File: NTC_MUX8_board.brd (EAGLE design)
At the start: 76.2 x 63.5 mm, 67 parts, among them IC1 NINA-B306-00B-00, IC2 INA126E, IC3 MCP6001T_SOT23, IC4 MAX8559ETAAA+T, J1 USB4105-GF-A, J2 1761681-7, J3 DM3CS-SF-PEJMS, J4 DNP, J7 52808-2071, U1 TMUX1208PWR, U2 TMUX1208PWR, U3 TMUX1208PWR, U4 TMUX1208PWR, X1 22-23-2021

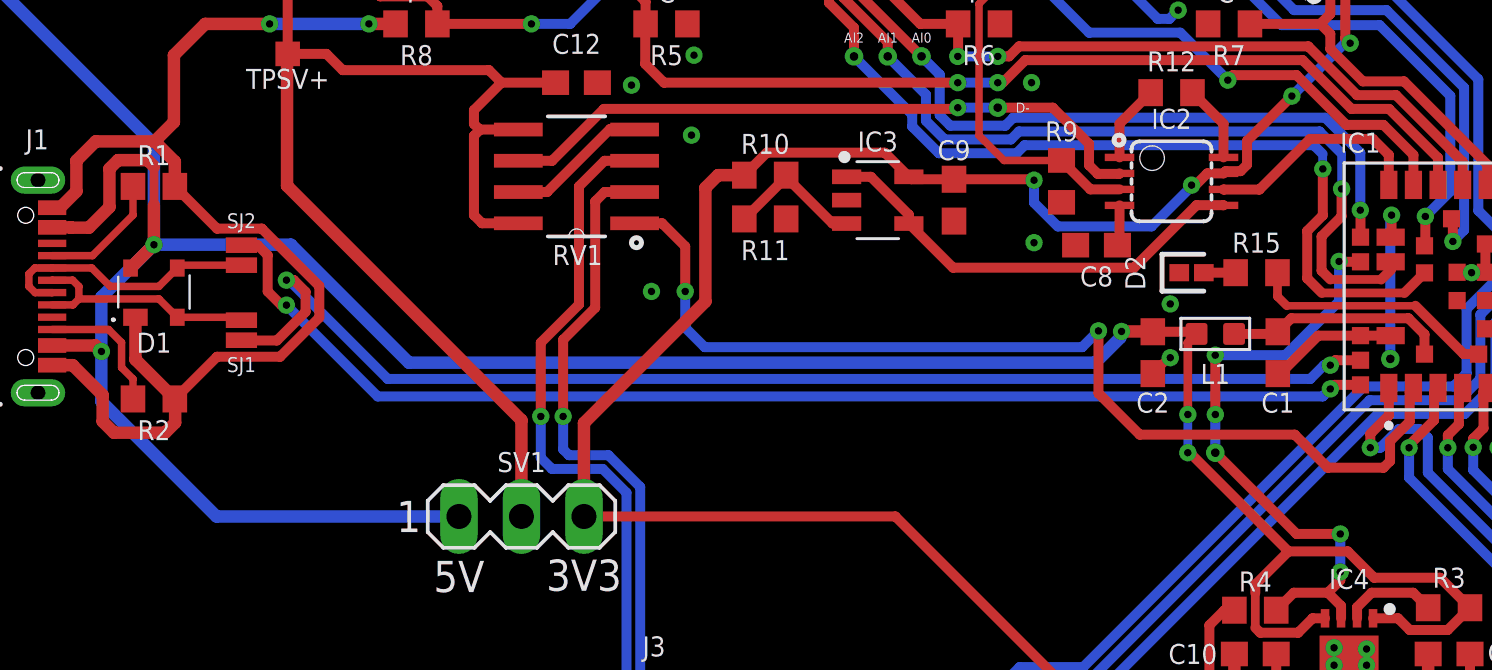
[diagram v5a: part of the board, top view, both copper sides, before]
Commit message: minor corrections
corrección v en seguidor
y pistas
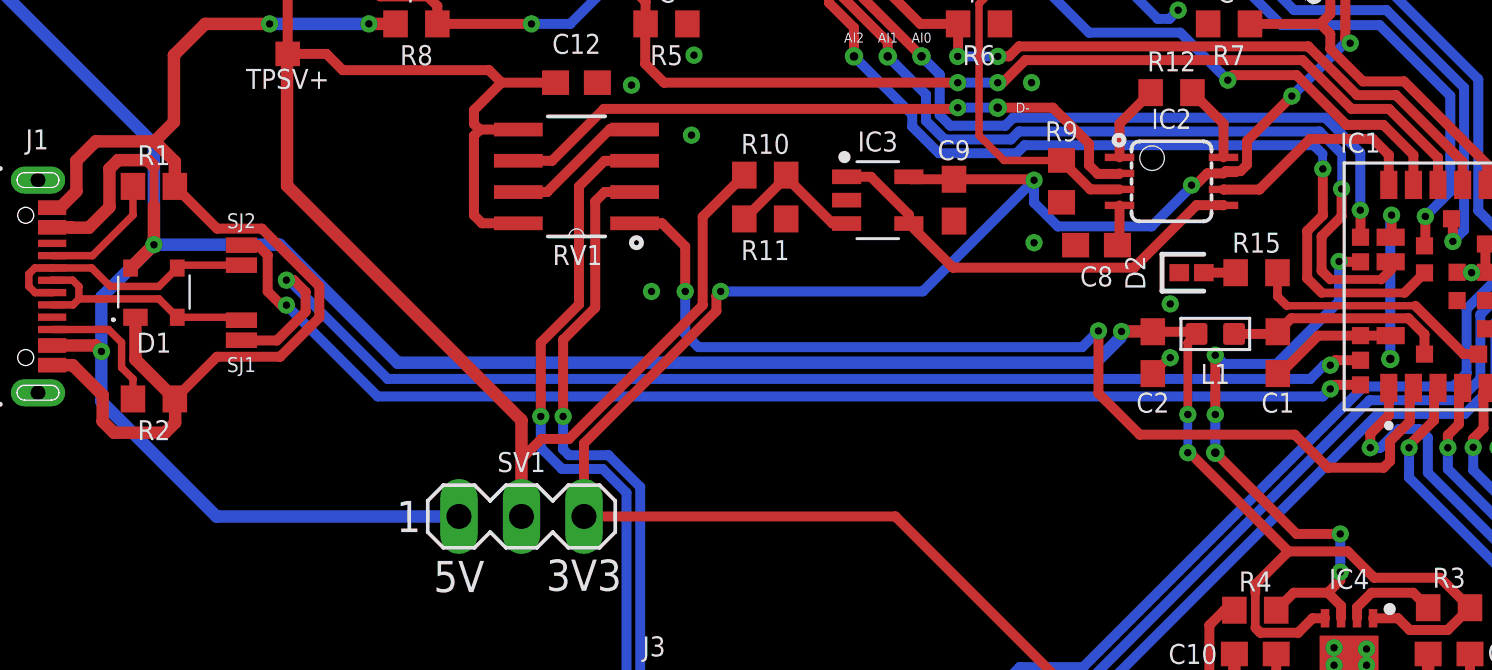
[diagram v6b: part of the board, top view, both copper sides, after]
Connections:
- net 3V3_2: no longer R10.1
- net VSEL: now also R10.1
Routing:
- net VSEL: track 104.3 -> 122.6 mm
- net 3V3_2: track 157.8 -> 159.3 mm, vias 7 -> 8
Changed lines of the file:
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@@
 <drawing>
 <settings>
-<setting alwaysvectorfont="yes"/>
+<setting alwaysvectorfont="no"/>
 <setting verticaltext="up"/>
 </settings>
@@
 <wire x1="9.0548" y1="29.35" x2="9.2964" y2="29.1084" width="0.508" layer="1"/>
 <wire x1="7.295" y1="29.35" x2="9.0548" y2="29.35" width="0.508" layer="1"/>
-<wire x1="11.43" y1="33.446" x2="16.9984" y2="33.446" width="0.508" layer="16"/>
-<wire x1="16.9984" y1="33.446" x2="21.7932" y2="28.6512" width="0.508" layer="16"/>
-<wire x1="49.6824" y1="28.6512" x2="21.7932" y2="28.6512" width="0.508" layer="16"/>
+<wire x1="11.43" y1="33.446" x2="16.5412" y2="33.446" width="0.508" layer="16"/>
+<wire x1="16.5412" y1="33.446" x2="21.336" y2="28.6512" width="0.508" layer="16"/>
+<wire x1="49.6824" y1="28.6512" x2="21.336" y2="28.6512" width="0.508" layer="16"/>
 <wire x1="50.6984" y1="29.6672" x2="49.6824" y2="28.6512" width="0.508" layer="16"/>
 <wire x1="50.6984" y1="29.8704" x2="50.6984" y2="29.6672" width="0.508" layer="16"/>
@@
 <contactref element="J5" pad="7"/>
 <contactref element="IC2" pad="7"/>
-<contactref element="R10" pad="1"/>
 <contactref element="IC3" pad="5"/>
 <contactref element="C9" pad="1"/>
@@
 <wire x1="55.3348" y1="15.0368" x2="55.3348" y2="14.6304" width="0.508" layer="1"/>
 <contactref element="SV1" pad="3"/>
-<wire x1="28.9052" y1="22.4028" x2="28.9052" y2="26.1992" width="0.508" layer="1"/>
-<wire x1="34.3544" y1="36.2712" x2="33.8396" y2="35.7564" width="0.508" layer="1"/>
-<wire x1="33.8396" y1="35.7564" x2="33.8396" y2="31.1336" width="0.508" layer="1"/>
-<wire x1="33.8396" y1="31.1336" x2="28.9052" y2="26.1992" width="0.508" layer="1"/>
-<wire x1="34.3544" y1="36.2712" x2="35.4212" y2="36.2712" width="0.508" layer="1"/>
-<wire x1="35.4212" y1="36.2712" x2="36.3356" y2="37.1856" width="0.4064" layer="1"/>
-<wire x1="41.1272" y1="37.1856" x2="42.1076" y2="36.2052" width="0.4064" layer="1"/>
-<wire x1="36.3356" y1="37.1856" x2="41.1272" y2="37.1856" width="0.4064" layer="1"/>
+<wire x1="42.006" y1="36.2052" x2="42.1076" y2="36.2052" width="0.4064" layer="1"/>
 <wire x1="43.942" y1="36.1052" x2="42.2076" y2="36.1052" width="0.4064" layer="1"/>
 <wire x1="42.2076" y1="36.1052" x2="42.1076" y2="36.2052" width="0.4064" layer="1"/>
@@
 <wire x1="53.2892" y1="8.3594" x2="53.0578" y2="8.128" width="0.508" layer="1"/>
 <wire x1="53.0578" y1="8.128" x2="48.602" y2="8.128" width="0.508" layer="1"/>
+<wire x1="47.1932" y1="36.068" x2="42.672" y2="31.5468" width="0.4064" layer="16"/>
+<wire x1="42.672" y1="31.5468" x2="34.4626" y2="31.5468" width="0.4064" layer="16"/>
+<via x="34.4626" y="31.5468" extent="1-16" drill="0.3"/>
+<wire x1="34.4626" y1="31.5468" x2="34.2876" y2="31.3718" width="0.4064" layer="1"/>
+<wire x1="34.2876" y1="31.3718" x2="34.2876" y2="30.75413125" width="0.4064" layer="1"/>
+<wire x1="28.9052" y1="25.37173125" x2="28.9052" y2="22.4028" width="0.4064" layer="1"/>
+<wire x1="34.2876" y1="30.75413125" x2="28.9052" y2="25.37173125" width="0.4064" layer="1"/>
 </signal>
 <signal name="AIN0">
@@
 <wire x1="27.94" y1="44.704" x2="29.21" y2="45.974" width="0.4064" layer="16"/>
 <wire x1="29.21" y1="45.974" x2="44.8564" y2="45.974" width="0.4064" layer="16"/>
+<contactref element="R10" pad="1"/>
+<wire x1="26.3652" y1="22.4028" x2="26.3652" y2="24.7396" width="0.4064" layer="1"/>
+<wire x1="26.3652" y1="24.7396" x2="27.178" y2="25.5524" width="0.4064" layer="1"/>
+<wire x1="27.178" y1="25.5524" x2="28.2956" y2="25.5524" width="0.4064" layer="1"/>
+<wire x1="33.7288" y1="34.5788" x2="35.4212" y2="36.2712" width="0.4064" layer="1"/>
+<wire x1="28.2956" y1="25.5524" x2="33.7288" y2="30.9856" width="0.4064" layer="1"/>
+<wire x1="33.7288" y1="30.9856" x2="33.7288" y2="34.5788" width="0.4064" layer="1"/>
 </signal>
 <signal name="N$4">
@@
 <via x="49.8122" y="29.9438" extent="1-16" drill="0.3"/>
 <wire x1="49.8122" y1="29.9438" x2="49.1518" y2="29.2834" width="0.4064" layer="16"/>
-<wire x1="49.1518" y1="29.2834" x2="33.8102" y2="29.2834" width="0.4064" layer="16"/>
-<wire x1="33.8102" y1="29.2834" x2="33.02" y2="30.0736" width="0.4064" layer="16"/>
-<wire x1="33.02" y1="30.0736" x2="33.02" y2="31.5468" width="0.4064" layer="16"/>
+<wire x1="49.1518" y1="29.2834" x2="33.5562" y2="29.2834" width="0.4064" layer="16"/>
+<wire x1="33.5562" y1="29.2834" x2="33.02" y2="29.8196" width="0.4064" layer="16"/>
+<wire x1="33.02" y1="29.8196" x2="33.02" y2="31.5468" width="0.4064" layer="16"/>
 <via x="33.02" y="31.5468" extent="1-16" drill="0.3"/>
 <wire x1="33.02" y1="31.5468" x2="33.02" y2="33.3756" width="0.4064" layer="1"/>
@@
 <wire x1="27.1498" y1="29.464" x2="27.1498" y2="26.4668" width="0.4064" layer="1"/>
 <via x="27.1498" y="26.4668" extent="1-16" drill="0.3"/>
-<wire x1="27.607" y1="24.3332" x2="27.1498" y2="24.7904" width="0.4064" layer="16"/>
-<wire x1="27.1498" y1="26.4668" x2="27.1498" y2="24.7904" width="0.4064" layer="16"/>
-<wire x1="27.607" y1="24.3332" x2="29.6672" y2="24.3332" width="0.4064" layer="16"/>
+<wire x1="28.0134" y1="24.3332" x2="27.1498" y2="25.1968" width="0.4064" layer="16"/>
+<wire x1="27.1498" y1="26.4668" x2="27.1498" y2="25.1968" width="0.4064" layer="16"/>
+<wire x1="28.0134" y1="24.3332" x2="29.6672" y2="24.3332" width="0.4064" layer="16"/>
 <wire x1="29.6672" y1="24.3332" x2="30.6324" y2="23.368" width="0.4064" layer="16"/>
 <via x="38.9" y="2.54" extent="1-16" drill="0.3"/>
@@
 <via x="59.5884" y="32.766" extent="1-16" drill="0.3"/>
 <wire x1="59.5884" y1="32.766" x2="59.5884" y2="31.1404" width="0.4064" layer="16"/>
-<wire x1="59.5884" y1="31.1404" x2="57.404" y2="28.956" width="0.4064" layer="16"/>
-<wire x1="54.5592" y1="28.956" x2="57.404" y2="28.956" width="0.4064" layer="16"/>
+<wire x1="59.5884" y1="31.1404" x2="57.0484" y2="28.6004" width="0.4064" layer="16"/>
+<wire x1="57.0484" y1="28.6004" x2="54.9148" y2="28.6004" width="0.4064" layer="16"/>
+<wire x1="54.5592" y1="28.956" x2="54.9148" y2="28.6004" width="0.4064" layer="16"/>
 <via x="54.5592" y="28.956" extent="1-16" drill="0.3"/>
 <wire x1="54.5592" y1="28.956" x2="54.5592" y2="26.5458" width="0.4064" layer="1"/>

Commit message: test points on front end
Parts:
- added D+, D-, VREF, V_ANLG: TESTPOINT_TPS-SMD-10SN, 52101-101-REV-A_v16:TESTPOINT_SMD-10SN
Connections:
- net D+: now also D+.TP
- net D-: now also D-.TP
- net V_ANALOG: now also V_ANLG.TP
- net V_REF: now also VREF.TP
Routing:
- net V_REF: track 18.1 -> 21.1 mm
- net 3V3_2: track 159.3 -> 157.3 mm
- net D-: track 27.0 -> 28.2 mm
- net V_ANALOG: track 9.06 -> 9.82 mm
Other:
- board text removed: "D-"

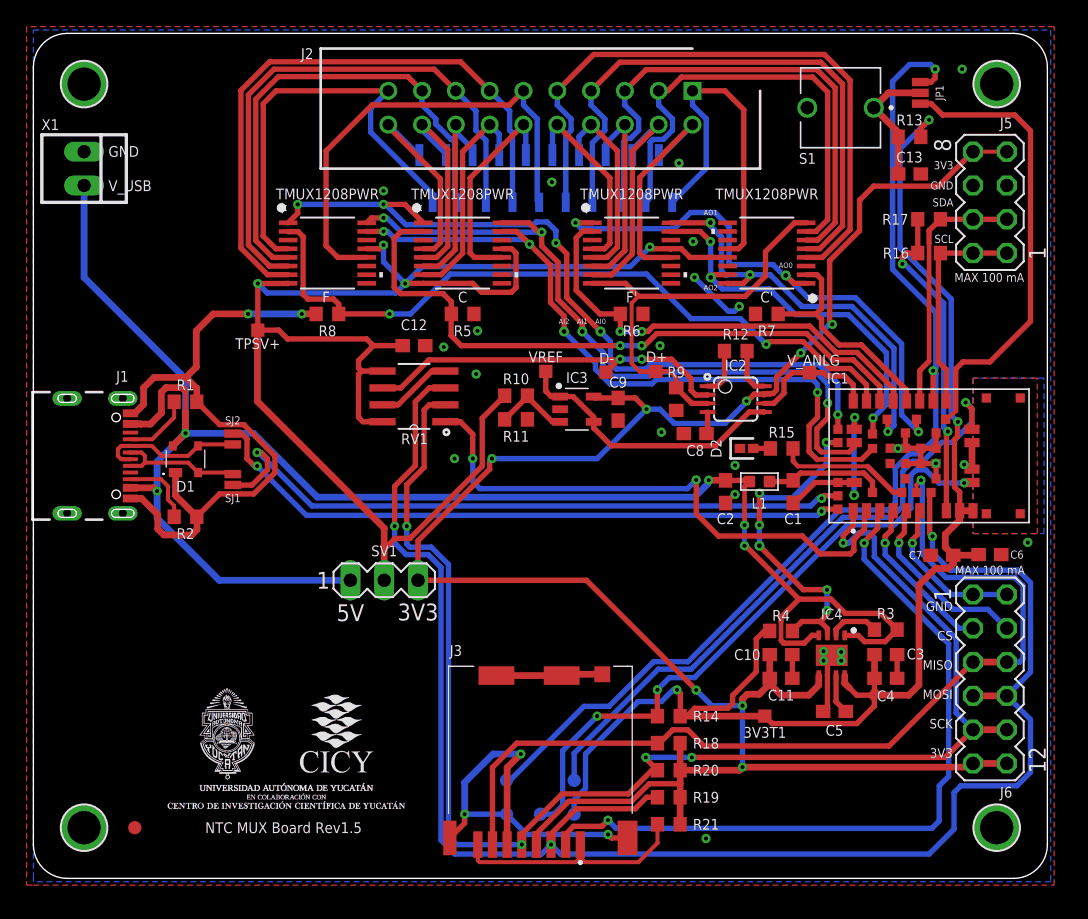
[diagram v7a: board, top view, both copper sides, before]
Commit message: teardrops en vias y pines
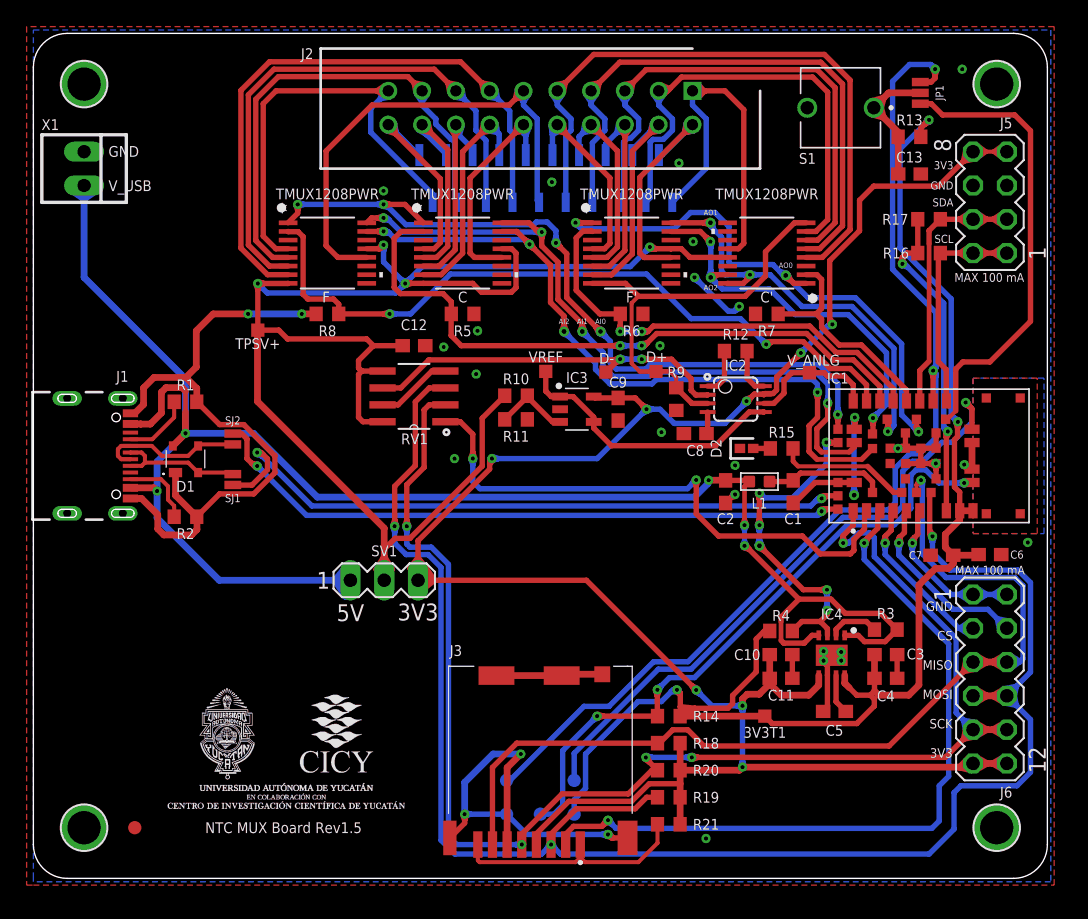
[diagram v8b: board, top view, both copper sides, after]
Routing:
- net 3V3_2: track 157.3 -> 199.5 mm
- net GND: track 143.4 -> 172.7 mm
- net SPI_SCK: track 107.7 -> 130.4 mm
- net SPI_MOSI: track 129.3 -> 148.6 mm
- net VSEL: track 122.6 -> 136.8 mm
- net V_EN: track 25.4 -> 39.6 mm
- net V_USB: track 133.8 -> 147.7 mm
- net SPI_MISO: track 70.8 -> 84.3 mm
- net AIN0: track 58.7 -> 71.7 mm
- net AIN2: track 54.6 -> 65.4 mm
- net AIN1: track 55.3 -> 66.0 mm
- net AOUT2: track 29.4 -> 38.0 mm
- net AOUT0: track 42.0 -> 50.7 mm
- net I2C_SCL: track 16.4 -> 24.9 mm
- net I2C_SDA: track 19.3 -> 27.7 mm
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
